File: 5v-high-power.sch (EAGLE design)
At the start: 31 parts, among them IC1 LM2576, J1 Bypass, J2 En, J3 12v, J4 5V Out, J5 LEN EN, J6 POWERPOLE_POWER10AWG, J7 POWERPOLE_POWER10AWG, Q1 SI4532ADY

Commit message: changed to correct powerpole version added current rating onto docu layer
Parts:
- J6, J7: value POWERPOLE_POWER10AWG -> POWERPOLE_POWER25A; device powerpoles:POWERPOLE_POWER10AWG -> powerpoles:POWERPOLE_POWER25A
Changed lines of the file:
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@@
 <part name="FRAME1" library="frames" deviceset="A4L-LOC" device=""/>
 <part name="J3" library="farnell-parts" deviceset="2-PIN-MOLEX" device="" value="12v"/>
-<part name="J6" library="powerpoles" deviceset="POWERPOLE_POWER" device="10AWG"/>
-<part name="J7" library="powerpoles" deviceset="POWERPOLE_POWER" device="10AWG"/>
+<part name="J6" library="powerpoles" deviceset="POWERPOLE_POWER" device="25A" value="POWERPOLE_POWER25A"/>
+<part name="J7" library="powerpoles" deviceset="POWERPOLE_POWER" device="25A" value="POWERPOLE_POWER25A"/>
 </parts>
 <sheets>

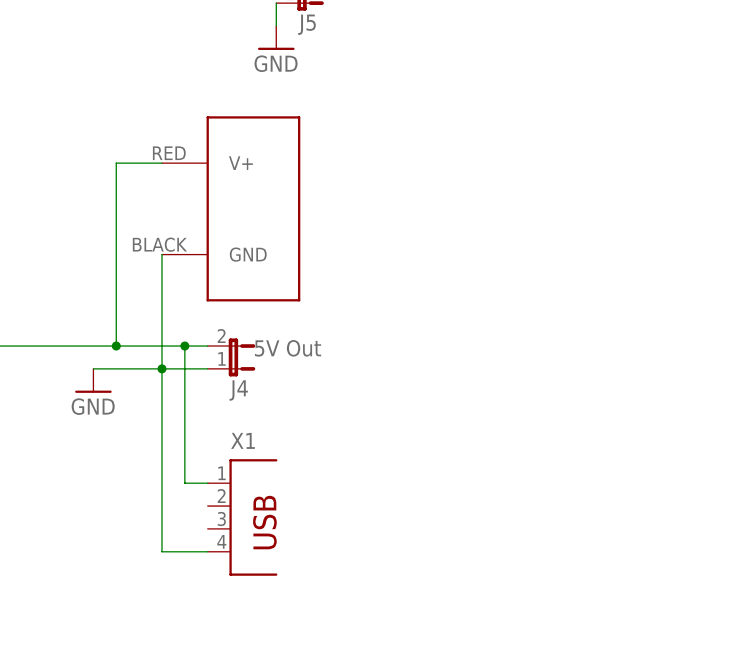
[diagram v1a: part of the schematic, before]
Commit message: Added additional USB footprints and rotated some powerpoles
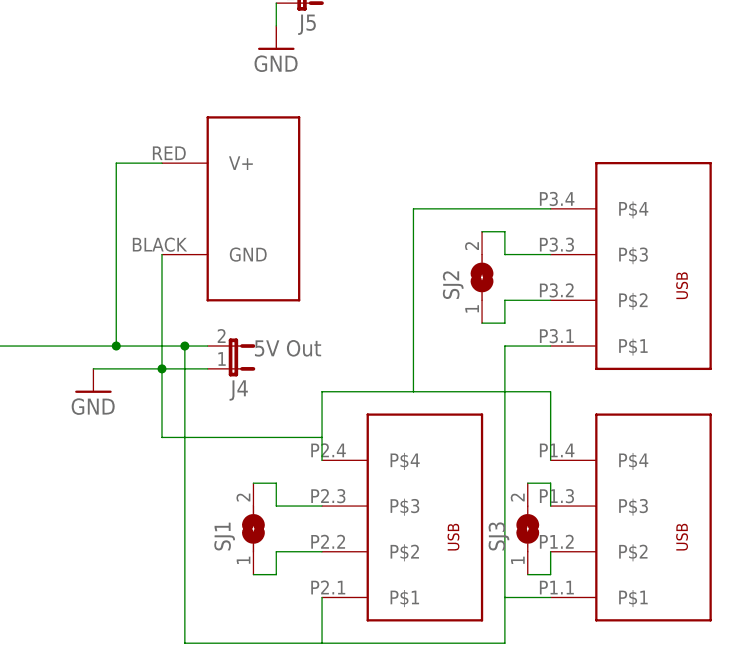
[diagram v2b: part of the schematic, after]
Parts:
- removed X1: (no value), con-berg:PN87520
- added SJ1, SJ2, SJ3: (no value), jumper:SJ
- added U$2: USB_DUAL_VERT+HORIZTRIPPLE, power:USB_DUAL_VERT+HORIZTRIPPLE
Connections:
- new net N$3: SJ1.2, U$2G$2.P$3
- new net N$4: SJ1.1, U$2G$2.P$2
- new net N$5: SJ2.2, U$2G$3.P$3
- new net N$6: SJ2.1, U$2G$3.P$2
- new net N$7: SJ3.2, U$2G$1.P$3
- new net N$8: SJ3.1, U$2G$1.P$2
- net 5V: now also U$2G$1.P$1, U$2G$2.P$1, U$2G$3.P$1; no longer X1.1
- net GND: now also U$2G$1.P$4, U$2G$2.P$4, U$2G$3.P$4; no longer X1.4
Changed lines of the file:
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@@
 <?xml version="1.0" encoding="utf-8"?>
 <!DOCTYPE eagle SYSTEM "eagle.dtd">
-<eagle version="6.5.0">
+<eagle version="6.4">
 <drawing>
 <settings>
@@
 <part name="P+3" library="supply1" deviceset="VCC" device=""/>
 <part name="D1" library="diode" deviceset="DIODE-" device="SMB"/>
-<part name="X1" library="con-berg" deviceset="PN87520" device=""/>
 <part name="GND" library="testpad" deviceset="TP" device="B1,27" value="5V B"/>
 <part name="FRAME1" library="frames" deviceset="A4L-LOC" device=""/>
@@
 <part name="J6" library="powerpoles" deviceset="POWERPOLE_POWER" device="25A" value="POWERPOLE_POWER25A"/>
 <part name="J7" library="powerpoles" deviceset="POWERPOLE_POWER" device="25A" value="POWERPOLE_POWER25A"/>
+<part name="U$2" library="power" deviceset="USB_DUAL_VERT+HORIZ" device="TRIPPLE"/>
+<part name="SJ1" library="jumper" deviceset="SJ" device=""/>
+<part name="SJ2" library="jumper" deviceset="SJ" device=""/>
+<part name="SJ3" library="jumper" deviceset="SJ" device=""/>
 </parts>
 <sheets>
@@
 <instance part="P+3" gate="VCC" x="124.46" y="116.84"/>
 <instance part="D1" gate="G$1" x="93.98" y="114.3"/>
-<instance part="X1" gate="G$1" x="198.12" y="40.64"/>
 <instance part="GND" gate="G$1" x="48.26" y="63.5"/>
 <instance part="FRAME1" gate="G$1" x="0" y="0"/>
@@
 <instance part="J6" gate="G$1" x="200.66" y="76.2"/>
 <instance part="J7" gate="G$1" x="76.2" y="129.54" rot="MR0"/>
+<instance part="U$2" gate="G$1" x="238.76" y="40.64"/>
+<instance part="U$2" gate="G$2" x="213.36" y="40.64"/>
+<instance part="U$2" gate="G$3" x="238.76" y="68.58"/>
+<instance part="SJ1" gate="1" x="200.66" y="40.64" rot="R90"/>
+<instance part="SJ2" gate="1" x="226.06" y="68.58" rot="R90"/>
+<instance part="SJ3" gate="1" x="231.14" y="40.64" rot="R90"/>
 </instances>
 <busses>
@@
 <pinref part="GND1" gate="1" pin="GND"/>
 <wire x1="195.58" y1="58.42" x2="190.5" y2="58.42" width="0.1524" layer="91"/>
-<pinref part="X1" gate="G$1" pin="4"/>
 <wire x1="190.5" y1="58.42" x2="182.88" y2="58.42" width="0.1524" layer="91"/>
-<wire x1="195.58" y1="38.1" x2="190.5" y2="38.1" width="0.1524" layer="91"/>
-<wire x1="190.5" y1="38.1" x2="190.5" y2="58.42" width="0.1524" layer="91"/>
 <junction x="190.5" y="58.42"/>
 <pinref part="J6" gate="G$1" pin="GND"/>
+<wire x1="190.5" y1="50.8" x2="190.5" y2="58.42" width="0.1524" layer="91"/>
 <wire x1="190.5" y1="71.12" x2="190.5" y2="58.42" width="0.1524" layer="91"/>
+<pinref part="U$2" gate="G$3" pin="P$4"/>
+<wire x1="233.68" y1="76.2" x2="218.44" y2="76.2" width="0.1524" layer="91"/>
+<wire x1="218.44" y1="76.2" x2="218.44" y2="55.88" width="0.1524" layer="91"/>
+<pinref part="U$2" gate="G$1" pin="P$4"/>
+<wire x1="218.44" y1="55.88" x2="233.68" y2="55.88" width="0.1524" layer="91"/>
+<wire x1="233.68" y1="55.88" x2="233.68" y2="48.26" width="0.1524" layer="91"/>
+<pinref part="U$2" gate="G$2" pin="P$4"/>
+<wire x1="218.44" y1="55.88" x2="208.28" y2="55.88" width="0.1524" layer="91"/>
+<wire x1="208.28" y1="55.88" x2="208.28" y2="50.8" width="0.1524" layer="91"/>
+<wire x1="208.28" y1="50.8" x2="208.28" y2="48.26" width="0.1524" layer="91"/>
+<wire x1="208.28" y1="50.8" x2="190.5" y2="50.8" width="0.1524" layer="91"/>
 </segment>
 <segment>
@@
 <pinref part="C5" gate="G$1" pin="+"/>
 <pinref part="J4" gate="G$1" pin="2"/>
-<pinref part="X1" gate="G$1" pin="1"/>
-<wire x1="195.58" y1="45.72" x2="193.04" y2="45.72" width="0.1524" layer="91"/>
-<wire x1="193.04" y1="45.72" x2="193.04" y2="60.96" width="0.1524" layer="91"/>
 <junction x="193.04" y="60.96"/>
 <pinref part="J6" gate="G$1" pin="V+"/>
@@
 <wire x1="185.42" y1="81.28" x2="185.42" y2="60.96" width="0.1524" layer="91"/>
 <junction x="185.42" y="60.96"/>
+<pinref part="U$2" gate="G$3" pin="P$1"/>
+<wire x1="233.68" y1="60.96" x2="228.6" y2="60.96" width="0.1524" layer="91"/>
+<wire x1="228.6" y1="60.96" x2="228.6" y2="33.02" width="0.1524" layer="91"/>
+<pinref part="U$2" gate="G$1" pin="P$1"/>
+<wire x1="228.6" y1="33.02" x2="233.68" y2="33.02" width="0.1524" layer="91"/>
+<wire x1="228.6" y1="33.02" x2="228.6" y2="27.94" width="0.1524" layer="91"/>
+<pinref part="U$2" gate="G$2" pin="P$1"/>
+<wire x1="228.6" y1="27.94" x2="208.28" y2="27.94" width="0.1524" layer="91"/>
+<wire x1="208.28" y1="27.94" x2="208.28" y2="33.02" width="0.1524" layer="91"/>
+<wire x1="208.28" y1="27.94" x2="193.04" y2="27.94" width="0.1524" layer="91"/>
+<wire x1="193.04" y1="27.94" x2="193.04" y2="60.96" width="0.1524" layer="91"/>
 </segment>
 <segment>
@@
 </segment>
 </net>
+<net name="N$3" class="0">
+<segment>
+<pinref part="U$2" gate="G$2" pin="P$3"/>
+<wire x1="208.28" y1="43.18" x2="203.2" y2="43.18" width="0.1524" layer="91"/>
+<wire x1="203.2" y1="43.18" x2="203.2" y2="45.72" width="0.1524" layer="91"/>
+<pinref part="SJ1" gate="1" pin="2"/>
+<wire x1="203.2" y1="45.72" x2="200.66" y2="45.72" width="0.1524" layer="91"/>
+</segment>
+</net>
+<net name="N$4" class="0">
+<segment>
+<pinref part="SJ1" gate="1" pin="1"/>
+<wire x1="200.66" y1="35.56" x2="203.2" y2="35.56" width="0.1524" layer="91"/>
+<wire x1="203.2" y1="35.56" x2="203.2" y2="38.1" width="0.1524" layer="91"/>
+<pinref part="U$2" gate="G$2" pin="P$2"/>
+<wire x1="203.2" y1="38.1" x2="208.28" y2="38.1" width="0.1524" layer="91"/>
+</segment>
+</net>
+<net name="N$5" class="0">
+<segment>
+<pinref part="SJ2" gate="1" pin="2"/>
+<wire x1="226.06" y1="73.66" x2="228.6" y2="73.66" width="0.1524" layer="91"/>
+<wire x1="228.6" y1="73.66" x2="228.6" y2="71.12" width="0.1524" layer="91"/>
+<pinref part="U$2" gate="G$3" pin="P$3"/>
+<wire x1="228.6" y1="71.12" x2="233.68" y2="71.12" width="0.1524" layer="91"/>
+</segment>
+</net>
+<net name="N$6" class="0">
+<segment>
+<pinref part="SJ2" gate="1" pin="1"/>
+<wire x1="226.06" y1="63.5" x2="228.6" y2="63.5" width="0.1524" layer="91"/>
+<wire x1="228.6" y1="63.5" x2="228.6" y2="66.04" width="0.1524" layer="91"/>
+<pinref part="U$2" gate="G$3" pin="P$2"/>
+<wire x1="228.6" y1="66.04" x2="233.68" y2="66.04" width="0.1524" layer="91"/>
+</segment>
+</net>
+<net name="N$7" class="0">
+<segment>
+<pinref part="SJ3" gate="1" pin="2"/>
+<pinref part="U$2" gate="G$1" pin="P$3"/>
+<wire x1="231.14" y1="45.72" x2="233.68" y2="45.72" width="0.1524" layer="91"/>
+<wire x1="233.68" y1="45.72" x2="233.68" y2="43.18" width="0.1524" layer="91"/>
+</segment>
+</net>
+<net name="N$8" class="0">
+<segment>
+<pinref part="SJ3" gate="1" pin="1"/>
+<pinref part="U$2" gate="G$1" pin="P$2"/>
+<wire x1="231.14" y1="35.56" x2="233.68" y2="35.56" width="0.1524" layer="91"/>
+<wire x1="233.68" y1="35.56" x2="233.68" y2="38.1" width="0.1524" layer="91"/>
+</segment>
+</net>
